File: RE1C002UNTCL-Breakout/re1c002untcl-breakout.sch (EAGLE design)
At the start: 2 parts, among them IC1 RE1C002UNTCL

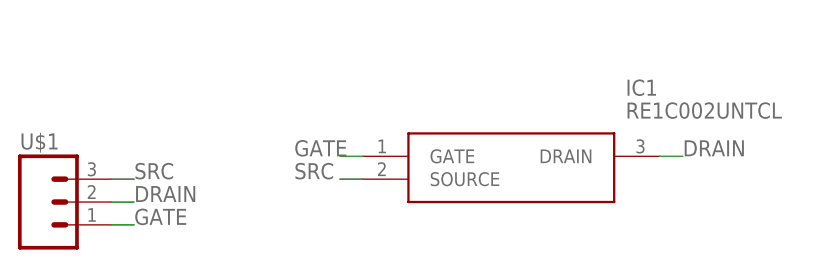
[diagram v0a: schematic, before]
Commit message: infinity mirror single apa102c
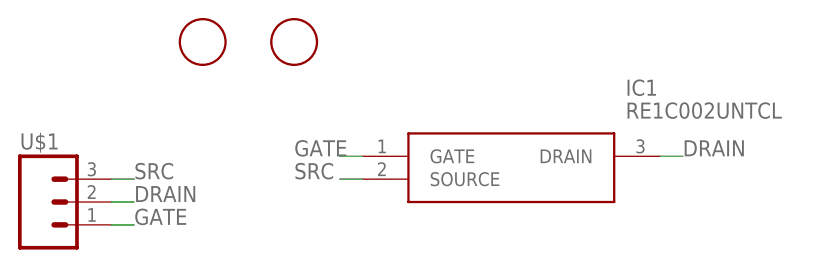
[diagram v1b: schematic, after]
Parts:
- added U$2, U$3: FIDUCIAL, adafruit:FIDUCIAL
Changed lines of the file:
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@@
 <part name="IC1" library="transitors" deviceset="RE1C002UNTCL" device=""/>
 <part name="U$1" library="connector" deviceset="M03" device=""/>
+<part name="U$2" library="adafruit" deviceset="FIDUCIAL" device=""/>
+<part name="U$3" library="adafruit" deviceset="FIDUCIAL" device=""/>
 </parts>
 <sheets>
@@
 <attribute name="NAME" x="25.4" y="76.962" size="1.778" layer="95"/>
 </instance>
+<instance part="U$2" gate="G$1" x="45.72" y="88.9" smashed="yes"/>
+<instance part="U$3" gate="G$1" x="55.88" y="88.9" smashed="yes"/>
 </instances>
 <busses>
